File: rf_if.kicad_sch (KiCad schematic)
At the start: 37 parts, among them U3 Adafruit_Si5351, U4 74LVC74, U5 74HCT244, U6 74HC4066, U7 74HC4066, U8 LM358

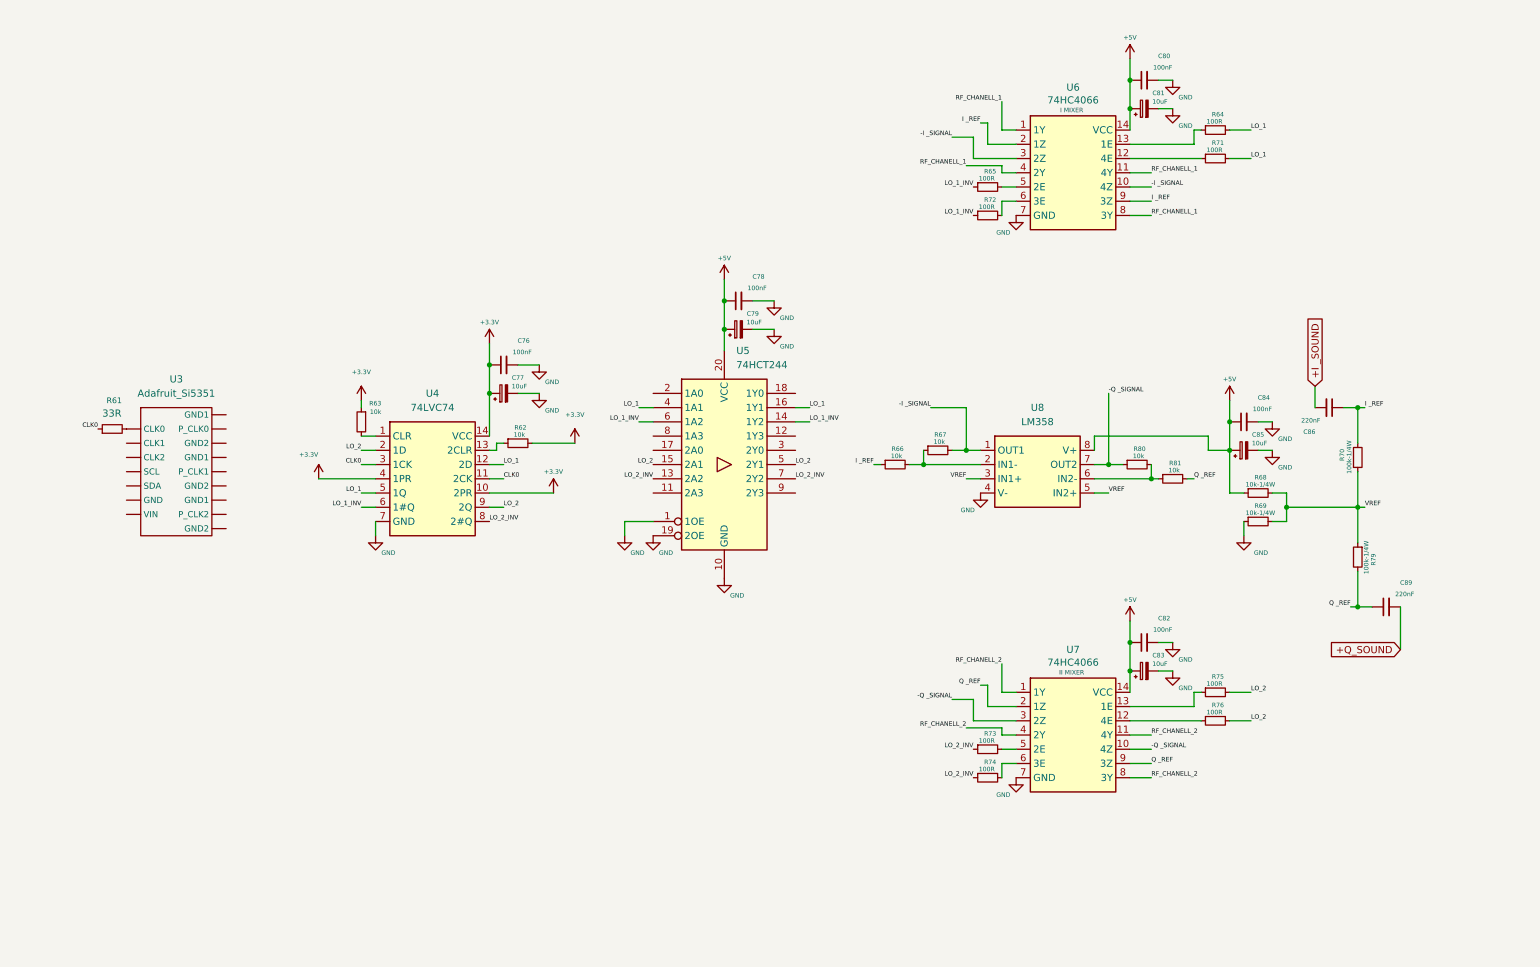
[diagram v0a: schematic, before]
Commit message: Resistive adder of mixers
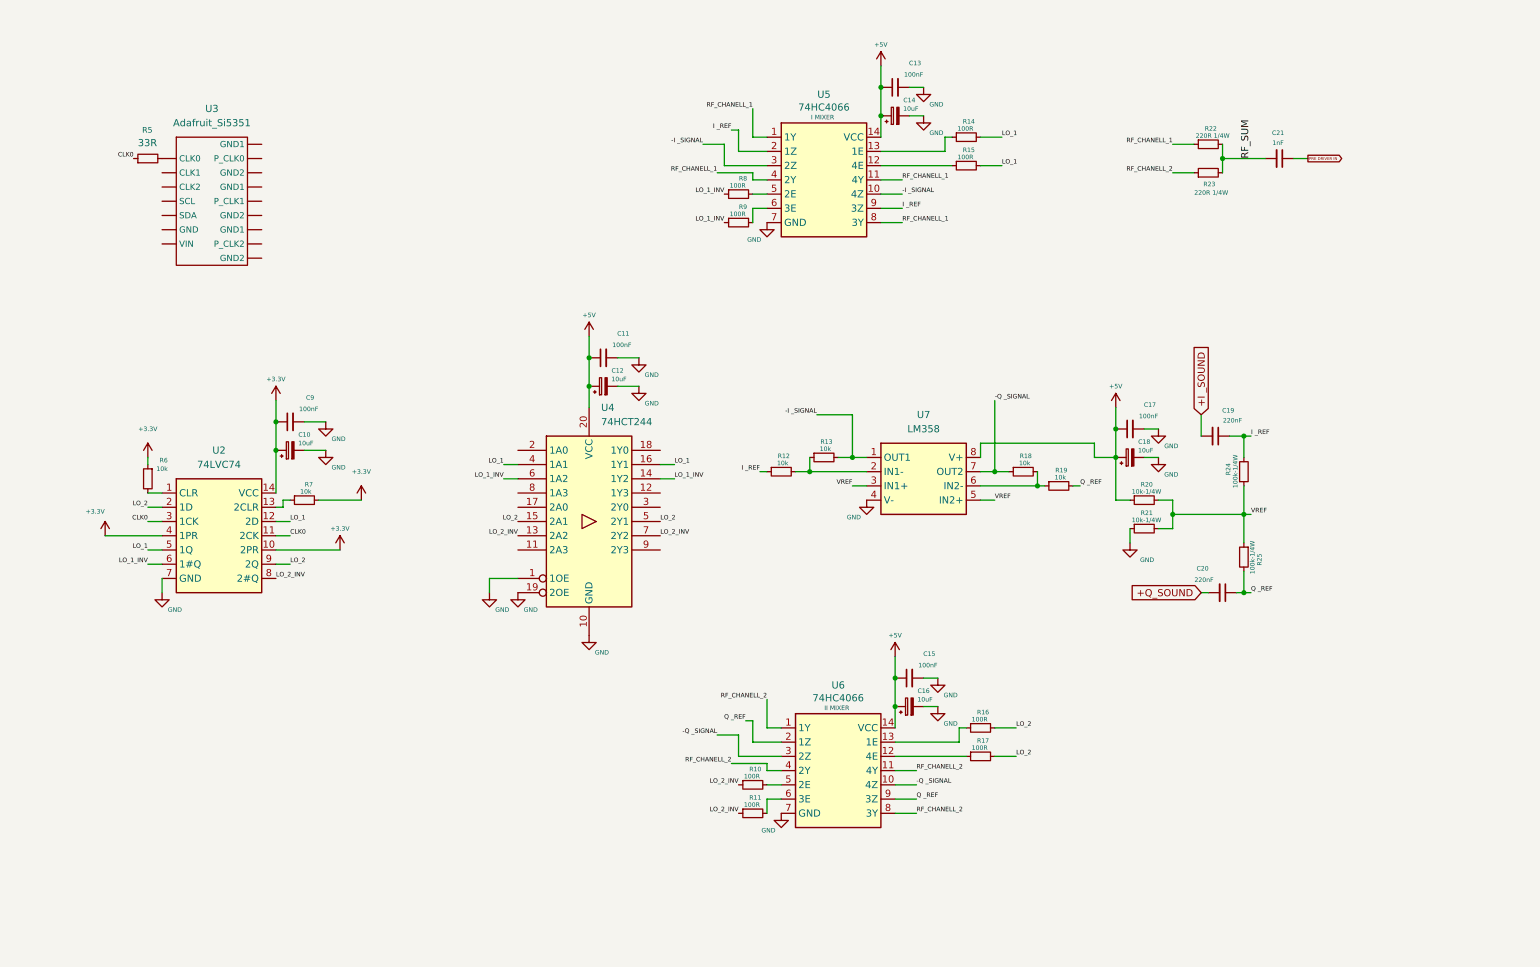
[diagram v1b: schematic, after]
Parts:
- added C21: 1nF, symbol Device:C_Small
- added R22, R23: 220R 1/4W, symbol Device:R_Small
- renumbered C77 to C10, C78 to C11, C79 to C12, C80 to C13, C81 to C14, C82 to C15, C83 to C16, C84 to C17, C85 to C18, C86 to C19, C89 to C20, C76 to C9, R73 to R10, R74 to R11, R66 to R12, R67 to R13, R64 to R14, R71 to R15, R75 to R16, R76 to R17, R80 to R18, R81 to R19, R68 to R20, R69 to R21, R70 to R24, R79 to R25, R61 to R5, R63 to R6, R62 to R7, R65 to R8, R72 to R9, U4 to U2, U5 to U4, U6 to U5, U7 to U6, U8 to U7
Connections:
- net RF_CHANELL_1: now also R22.1
- net RF_CHANELL_2: now also R23.1
- new net PRE DRIVER IN: C21.1
- new net RF_SUM: C21.2, R22.2, R23.2
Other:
- moved on the sheet: C10, C11, C12, C13, C14, C15, C16, C17, C18, C19, C20, C9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

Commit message: BPF Work 2
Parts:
- renumbered C9 to C24, C10 to C25, C11 to C26, C12 to C27, C13 to C28, C14 to C29, C15 to C30, C16 to C31, C17 to C32, C18 to C33, C19 to C34, C20 to C35, C21 to C36

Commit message: Mixer work
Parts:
- added IC1: SBL-1+, SBL1, symbol omega:SBL-1+
- added Q33: 2SC5171, Package_TO_SOT_THT:TO-220-3_Vertical, symbol Transistor_BJT:2SC1945
- added R87: 560R/No Ind., symbol Device:R_Small
- added R88: 120R/No Ind., symbol Device:R_Small
- added R89: 10k, symbol Device:R_Small
- added R90: 1k8, symbol Device:R_Small
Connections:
- net GND: now also R88.1, R90.1
- new net: Q33.1 (B), R89.1, R90.2
- new net: Q33.3 (C), R87.2
- new net: Q33.2 (E), R88.2
- new net +12V_MAIN: R87.1, R89.2

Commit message: Mixer work 2
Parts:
- added C146, C147: 100nF, symbol Device:C_Small
- added C148: 4.7uF, symbol Device:C_Polarized_Small
- added R91: 51R/No Ind., symbol Device:R_Small
- added R92: 47R/No Ind., symbol Device:R_Small
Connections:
- net GND: now also C147.1, C148.2, R91.1
- net at Q33.1 (B), R89.1, R90.2: now also R92.2
- net at Q33.3 (C), R87.2: now also C147.2, C148.1
- new net: C146.2, R92.1
- new net BPF_OUT: C146.1, R91.2
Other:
- moved on the sheet: C24, C25, C26, C27, IC1, Q33, R6, R7, R87, R88, R89, R90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

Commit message: Mixer work 3
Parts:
- added C149: 4.7uF, symbol Device:C_Polarized_Small
- added C150, C151: 100nF, symbol Device:C_Small
- added Q34: 2N2219A, Package_TO_SOT_THT:TO-220-3_Vertical, symbol Transistor_BJT:2SC1945
- added R93: 330R/No Ind., symbol Device:R_Small
- added R94, R95: 47R/No Ind., symbol Device:R_Small
- Q33: value 2SC5171 -> 2N2219A
- R87: value 560R/No Ind. -> 620R/No Ind.
- R88: value 120R/No Ind. -> 150R/No Ind.
- R89: value 10k -> 6k2
- R90: value 1k8 -> 1k2
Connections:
- net +12V_MAIN: now also C149.1, C150.2, Q34.3 (C)
- net GND: now also IC1.2 (GROUND_1), IC1.5 (GROUND_2), IC1.6 (GROUND_3), IC1.7 (GROUND_4), C149.2, C150.1, R93.1
- net at C147.2, C148.1, Q33.3 (C)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: now also R94.1
- net at IC1.1 (RF): now also C151.2
- new net: C151.1, R95.1
- new net: Q34.1 (B), R94.2
- new net: Q34.2 (E), R93.2, R95.2
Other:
- moved on the sheet: C146, C147, C148, C28, C29, C30, C31, C36, IC1, Q33, R10, R11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

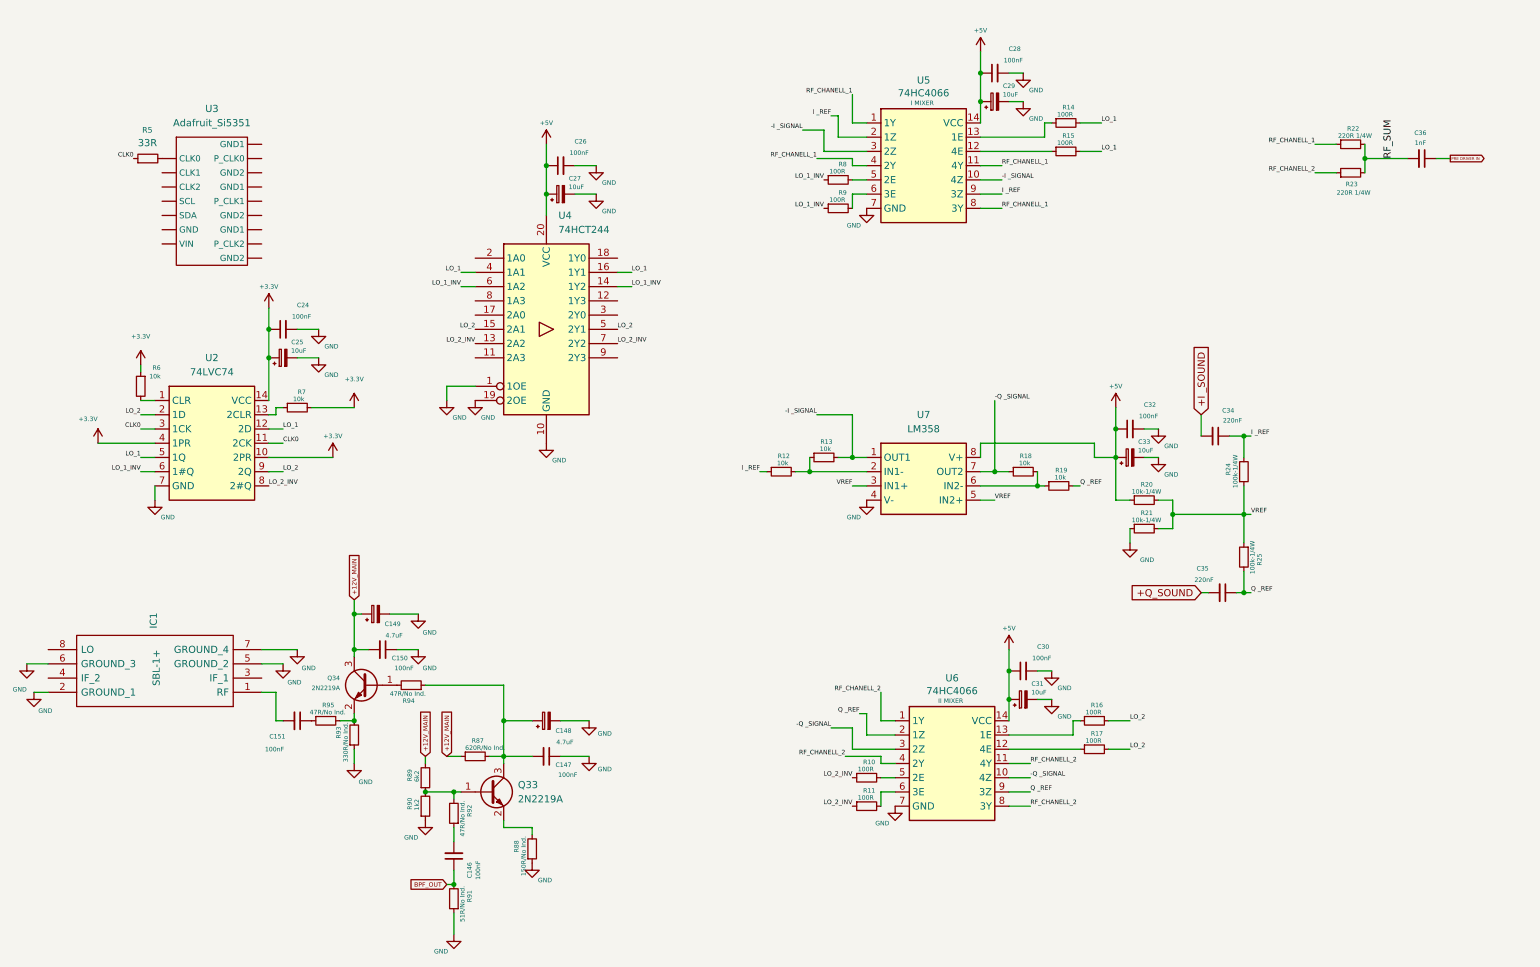
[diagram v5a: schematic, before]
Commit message: Rf RX amplifier, BPF RX
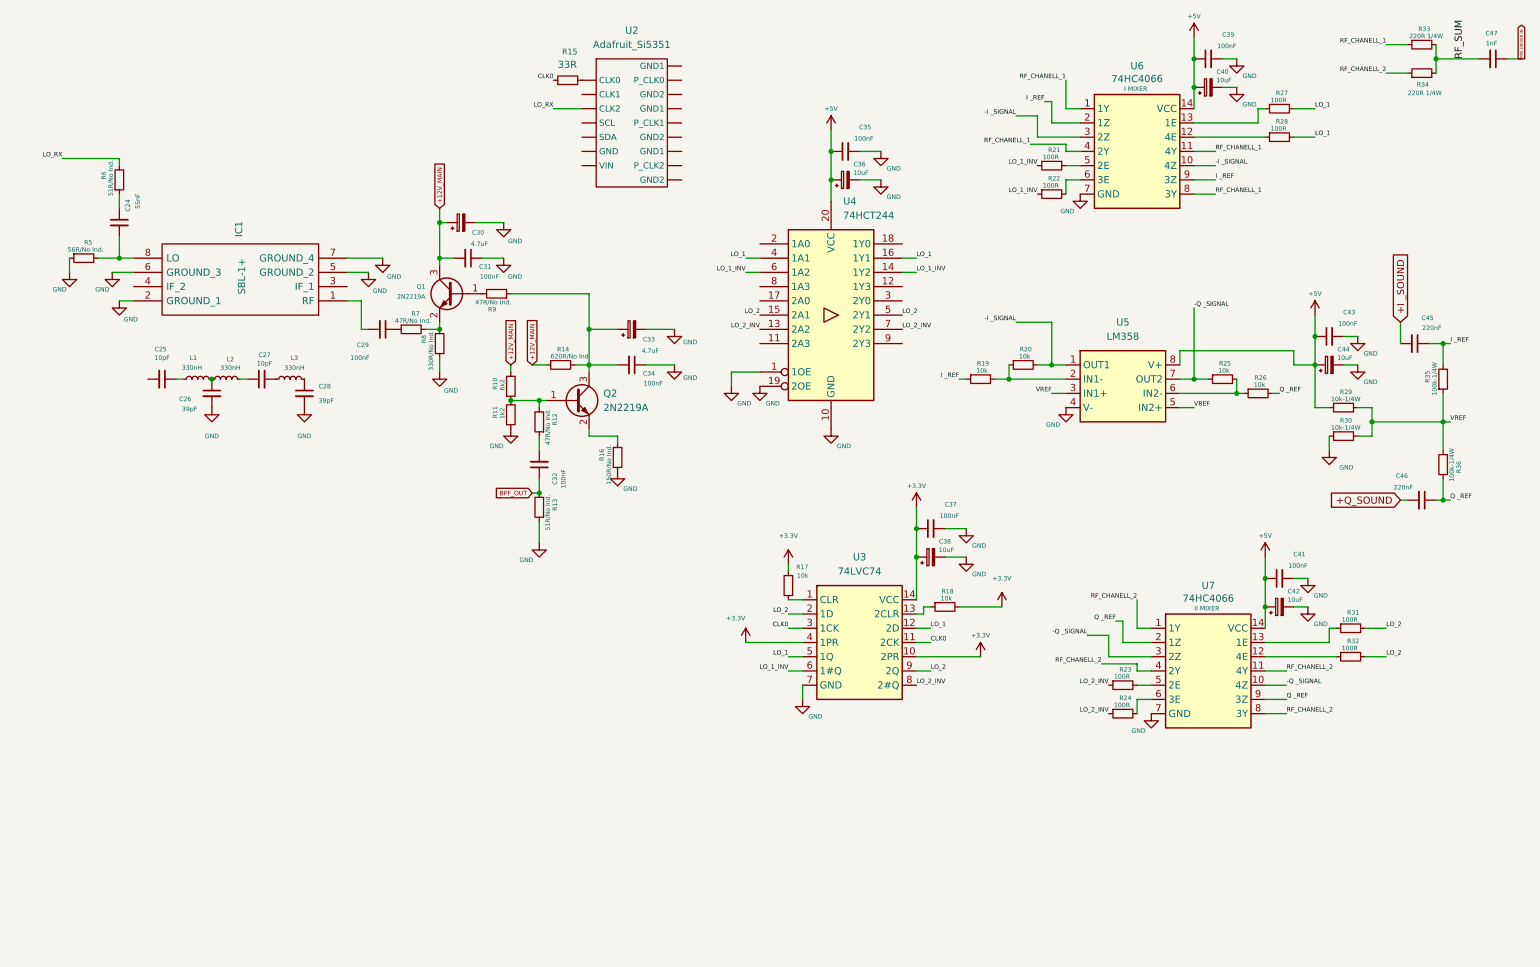
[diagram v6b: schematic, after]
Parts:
- added C24: 55nF, symbol Device:C_Small
- added C25, C27: 10pF, symbol Device:C_Small
- added C26, C28: 39pF, symbol Device:C_Small
- added L1, L2, L3: 330nH, symbol Device:L_Small
- added R5: 56R/No Ind., symbol Device:R_Small
- added R6: 51R/No Ind., symbol Device:R_Small
- renumbered C151 to C29, C149 to C30, C150 to C31, C146 to C32, C148 to C33, C147 to C34, C26 to C35, C27 to C36, C24 to C37, C25 to C38, C28 to C39, C29 to C40, C30 to C41, C31 to C42, C32 to C43, C33 to C44, C34 to C45, C35 to C46, C36 to C47, Q34 to Q1, Q33 to Q2, R89 to R10, R90 to R11, R92 to R12, R91 to R13, R87 to R14, R5 to R15, R88 to R16, R6 to R17, R7 to R18, R12 to R19, R13 to R20, R8 to R21, R9 to R22, R10 to R23, R11 to R24, R18 to R25, R19 to R26, R14 to R27, R15 to R28, R20 to R29, R21 to R30, R16 to R31, R17 to R32, R22 to R33, R23 to R34, R24 to R35, R25 to R36, R95 to R7, R93 to R8, R94 to R9, U3 to U2, U2 to U3, U7 to U5, U5 to U6, U6 to U7
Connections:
- net GND: now also C26.2, C28.2, R5.1
- net at IC1.8 (LO): now also C24.2, R5.2
- net LO_RX: now reaches U2. (GND2)
- net LO_RX: now also R6.2
- new net: C26.1, L1.2, L2.1
- new net: C27.1, L2.2
- new net: C25.1, L1.1
- new net: C28.1, L3.2
- new net: C24.1, R6.1
- new net: C27.2, L3.1
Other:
- moved on the sheet: C29, C30, C31, C32, C33, C34, C35, C36, C37, C38, C39, C40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

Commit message: RF Gain
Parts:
- added C24, C27, C31: 10nF, symbol Device:C_Small
- added C28: 10uF, symbol Device:C_Polarized_Small
- added C30: 100nF, symbol Device:C_Small
- added Q1: 2N5109, Package_TO_SOT_THT:TO-220-3_Vertical, symbol Transistor_BJT:2SC1945
- added R10: 82R/NoH/0.25W, symbol Device:R_Small
- added R11: 150R/NoH/0.5W, symbol Device:R_Small
- added R12, R9: 22R/NoH, symbol Device:R_Small
- added R13: 10R/No Ind., symbol Device:R_Small
- added R5: 3k3, symbol Device:R_Small
- added R6: 1k, symbol Device:R_Small
- added RV1: 500R, symbol Device:R_Potentiometer_Trim
- renumbered C24 to C25, C28 to C26, C27 to C29, C26 to C32, C25 to C33, C29 to C34, C30 to C35, C31 to C36, C32 to C37, C33 to C38, C34 to C39, C35 to C40, C36 to C41, C37 to C42, C38 to C43, C39 to C44, C40 to C45, C41 to C46, C42 to C47, C43 to C48, C44 to C49, C45 to C50, C46 to C51, C47 to C52, L3 to L1, L1 to L3, Q1 to Q2, Q2 to Q3, R7 to R14, R8 to R15, R10 to R16, R11 to R17, R9 to R18, R12 to R19, R13 to R20, R14 to R21, R15 to R22, R16 to R23, R17 to R24, R18 to R25, R19 to R26, R21 to R27, R22 to R28, R20 to R29, R23 to R30, R24 to R31, R25 to R32, R27 to R33, R28 to R34, R26 to R35, R31 to R36, R32 to R37, R29 to R38, R30 to R39, R33 to R40, R34 to R41, R35 to R42, R36 to R43, R5 to R7, R6 to R8, U6 to U5, U5 to U6
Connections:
- net +12V_MAIN: now also R11.2, R5.2
- net GND: now also IC1.4 (IF_2), C27.2, C28.2, C30.1, R10.1, R6.1, RV1.3
- net at C33.2: now also IC1.3 (IF_1)
- net IF_70M_IN: now reaches C26.1, L1.2
- net IF_70M_IN: now also C24.2, R9.2
- net at C34.2: now also R13.1; no longer IC1.1 (RF)
- new net: IC1.1 (RF), R13.2, RV1.1, RV1.2
- new net: C27.1, C28.1, Q1.3 (C), R11.1, R12.1
- new net: C31.2, R12.2
- new net: C30.2, Q1.2 (E), R10.2
- new net: C24.1, R5.1, R6.2
- new net: Q1.1 (B), R9.1
- new net IF_70M_OUT: C31.1
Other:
- moved on the sheet: C26, C29, C32, C33, C34, C35, C36, C37, C38, C39, C40, C41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

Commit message: AGC Work
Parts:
- added Q2: J310, symbol Device:Q_NJFET_DSG
- added R105: 100k/NoH, symbol Device:R_Small
- added R106: 1M/NoH, symbol Device:R_Small
- added U8: LM358, symbol omega:LM358
- renumbered Q2 to Q3, Q3 to Q4
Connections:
- net GND: now also Q2.2 (S), R106.2
- net IF_70M_OUT: now also Q2.1 (D)
- net IF_70M_IN: no longer names the net of C24.2, C26.1, L1.2, R9.2
- new net: Q2.3 (G), R105.2, R106.1
- new net: R105.1, U8.1 (OUT1)
- new net: U8.11 (NC), U8.4 (V-)
